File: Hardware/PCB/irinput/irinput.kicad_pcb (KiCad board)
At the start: 2 copper layers, 121 x 170.5 mm, 37 parts, among them J2 Synth_power_2x5, J3 Conn_01x06, J4 Conn_01x06, J5 AudioJack2, J6 AudioJack2, Q1 TOPS-050, SW1 SW_DPDT_x2, SW2 SW_SPDT, U1 TL074

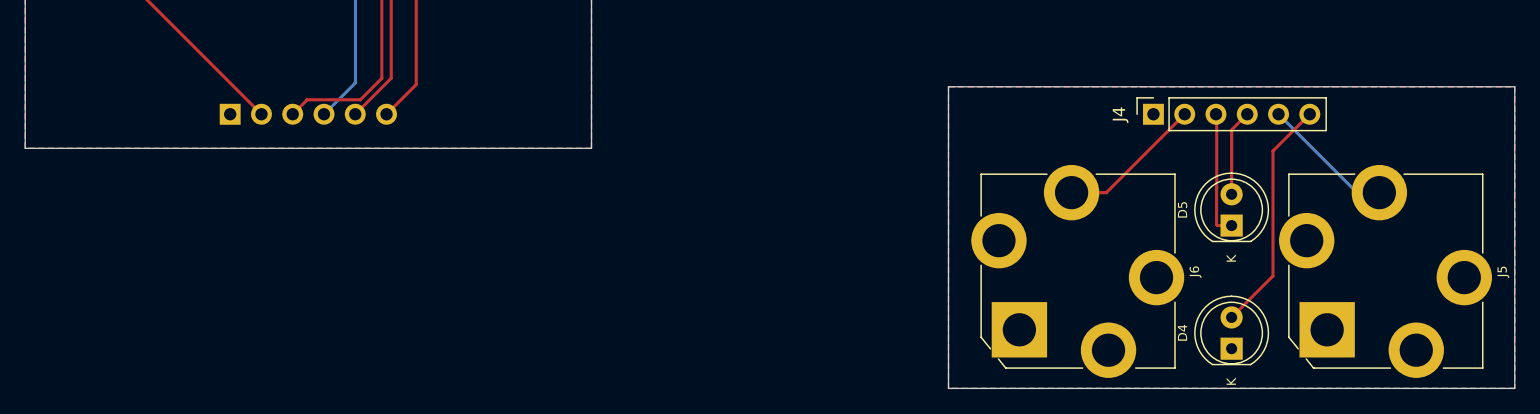
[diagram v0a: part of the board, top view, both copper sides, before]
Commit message: Revised schematic to buffer input to variable gain stage
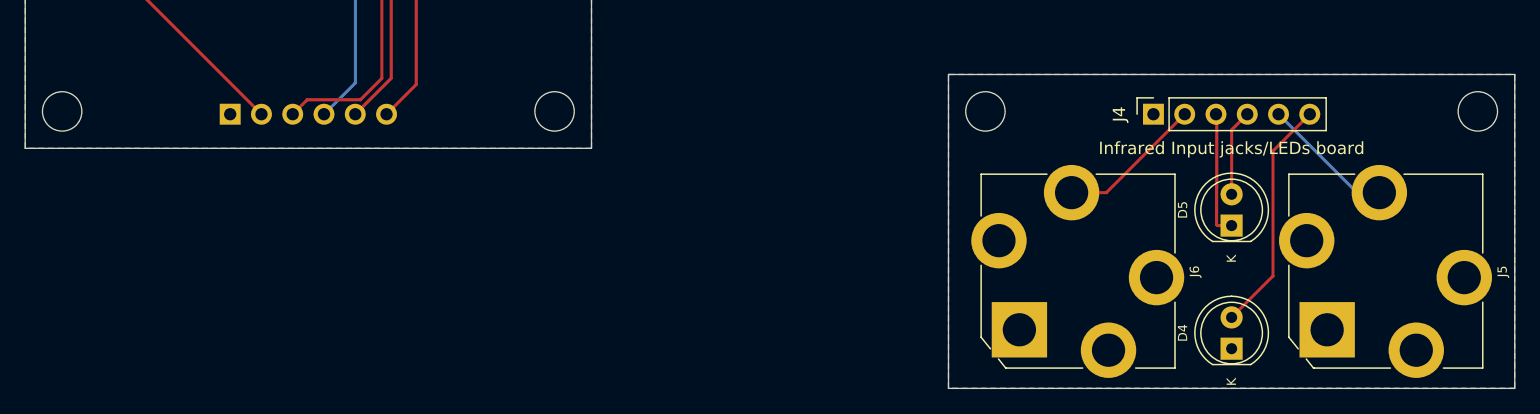
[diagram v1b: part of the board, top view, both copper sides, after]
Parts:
- added H1: MountingHole, ao_tht:MountingHole_3.2mm_M3, F.Cu at (80.0, 162.0)
- added H2: MountingHole, ao_tht:MountingHole_3.2mm_M3, F.Cu at (120.0, 162.0)
- added H3: MountingHole, ao_tht:MountingHole_3.2mm_M3, F.Cu at (155.0, 162.0)
- added H4: MountingHole, ao_tht:MountingHole_3.2mm_M3, F.Cu at (195.0, 162.0)
- moved B2 1.00 mm to (162.5, 159.0)
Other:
- outline, holes or cut-outs redrawn
- board text added: "Infrared Input"
- board text added: "Infrared Input jacks/LEDs board"
- board text added: "Main board"
- board text added: "Original design by Michael Barton Modifications by Rich Holmes Feb 2022"
- board text added: "https://www.bartonmusicalcircuits.com/irin/index.html https://github.com/holmesrichards/irinput"
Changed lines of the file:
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@@
   )
   (footprint "ao_tht:Board_Marker" (layer "F.Cu")
-    (at 162.5 160)
+    (at 162.5 159)
     (descr "Mark board for extraction")
     (property "Config" "DNF")
@@
     )
   )
+  (footprint "ao_tht:MountingHole_3.2mm_M3" (layer "F.Cu")
+    (at 80 162)
+    (descr "Mounting Hole 3.2mm, no annular, M3")
+    (tags "mounting hole 3.2mm no annular m3")
+    (property "Config" "DNF")
+    (property "Sheetfile" "irinput.kicad_sch")
+    (property "Sheetname" "")
+    (property "exclude_from_bom" "")
+    (attr exclude_from_pos_files exclude_from_bom)
+    (fp_text reference "H1" (at 0 -4.2) (layer "F.SilkS") hide
+      (effects (font (size 1 1) (thickness 0.15)))
+    )
+    (fp_text value "MountingHole" (at 0 4.2) (layer "F.Fab")
+      (effects (font (size 1 1) (thickness 0.15)))
+    )
+    (fp_text user "${REFERENCE}" (at 0.3 0) (layer "F.Fab") hide
+      (effects (font (size 1 1) (thickness 0.15)))
+    )
+    (fp_circle (center 0 0) (end 3.2 0) (layer "Cmts.User") (width 0.15) (fill none))
+    (fp_circle (center 0 0) (end 3.45 0) (layer "F.CrtYd") (width 0.05) (fill none))
+    (pad "" np_thru_hole circle locked (at 0 0) (size 3.2 3.2) (drill 3.2) (layers *.Cu *.Mask))
+  )
   (footprint "Connector_PinSocket_2.54mm:PinSocket_1x06_P2.54mm_Vertical" (layer "F.Cu")
     (at 168.65 162.23 90)
@@
     )
   )
+  (footprint "ao_tht:MountingHole_3.2mm_M3" (layer "F.Cu")
+    (at 195 162)
+    (descr "Mounting Hole 3.2mm, no annular, M3")
+    (tags "mounting hole 3.2mm no annular m3")
+    (property "Config" "DNF")
+    (property "Sheetfile" "irinput.kicad_sch")
+    (property "Sheetname" "")
+    (property "exclude_from_bom" "")
+    (attr exclude_from_pos_files exclude_from_bom)
+    (fp_text reference "H4" (at 0 -4.2) (layer "F.SilkS") hide
+      (effects (font (size 1 1) (thickness 0.15)))
+    )
+    (fp_text value "MountingHole" (at 0 4.2) (layer "F.Fab")
+      (effects (font (size 1 1) (thickness 0.15)))
+    )
+    (fp_text user "${REFERENCE}" (at 0.3 0) (layer "F.Fab") hide
+      (effects (font (size 1 1) (thickness 0.15)))
+    )
+    (fp_circle (center 0 0) (end 3.2 0) (layer "Cmts.User") (width 0.15) (fill none))
+    (fp_circle (center 0 0) (end 3.45 0) (layer "F.CrtYd") (width 0.05) (fill none))
+    (pad "" np_thru_hole circle locked (at 0 0) (size 3.2 3.2) (drill 3.2) (layers *.Cu *.Mask))
+  )
   (footprint "ao_tht:Potentiometer_Alpha_RD901F-40-00D_Single_Vertical_centered" (layer "F.Cu")
     (at 100 145)
@@
     )
   )
+  (footprint "ao_tht:MountingHole_3.2mm_M3" (layer "F.Cu")
+    (at 120 162)
+    (descr "Mounting Hole 3.2mm, no annular, M3")
+    (tags "mounting hole 3.2mm no annular m3")
+    (property "Config" "DNF")
+    (property "Sheetfile" "irinput.kicad_sch")
+    (property "Sheetname" "")
+    (property "exclude_from_bom" "")
+    (attr exclude_from_pos_files exclude_from_bom)
+    (fp_text reference "H2" (at 0 -4.2) (layer "F.SilkS") hide
+      (effects (font (size 1 1) (thickness 0.15)))
+    )
+    (fp_text value "MountingHole" (at 0 4.2) (layer "F.Fab")
+      (effects (font (size 1 1) (thickness 0.15)))
+    )
+    (fp_text user "${REFERENCE}" (at 0.3 0) (layer "F.Fab") hide
+      (effects (font (size 1 1) (thickness 0.15)))
+    )
+    (fp_circle (center 0 0) (end 3.2 0) (layer "Cmts.User") (width 0.15) (fill none))
+    (fp_circle (center 0 0) (end 3.45 0) (layer "F.CrtYd") (width 0.05) (fill none))
+    (pad "" np_thru_hole circle locked (at 0 0) (size 3.2 3.2) (drill 3.2) (layers *.Cu *.Mask))
+  )
+  (footprint "ao_tht:MountingHole_3.2mm_M3" (layer "F.Cu")
+    (at 155 162)
+    (descr "Mounting Hole 3.2mm, no annular, M3")
+    (tags "mounting hole 3.2mm no annular m3")
+    (property "Config" "DNF")
+    (property "Sheetfile" "irinput.kicad_sch")
+    (property "Sheetname" "")
+    (property "exclude_from_bom" "")
+    (attr exclude_from_pos_files exclude_from_bom)
+    (fp_text reference "H3" (at 0 -4.2) (layer "F.SilkS") hide
+      (effects (font (size 1 1) (thickness 0.15)))
+    )
+    (fp_text value "MountingHole" (at 0 4.2) (layer "F.Fab")
+      (effects (font (size 1 1) (thickness 0.15)))
+    )
+    (fp_text user "${REFERENCE}" (at 0.3 0) (layer "F.Fab") hide
+      (effects (font (size 1 1) (thickness 0.15)))
+    )
+    (fp_circle (center 0 0) (end 3.2 0) (layer "Cmts.User") (width 0.15) (fill none))
+    (fp_circle (center 0 0) (end 3.45 0) (layer "F.CrtYd") (width 0.05) (fill none))
+    (pad "" np_thru_hole circle locked (at 0 0) (size 3.2 3.2) (drill 3.2) (layers *.Cu *.Mask))
+  )
   (footprint "ao_tht:SPDT-toggle-switch-1M-series" (layer "F.Cu")
     (at 87.5 105 180)
@@
     (fp_line (start 11.21 -1.5) (end 11.21 1.5) (layer "B.CrtYd") (width 0.05))
     (fp_line (start -1.05 -1.5) (end 11.21 -1.5) (layer "B.CrtYd") (width 0.05))
+    (fp_line (start 1.93 1.25) (end 1.93 -1.25) (layer "B.Fab") (width 0.1))
     (fp_line (start 8.23 -1.25) (end 8.23 1.25) (layer "B.Fab") (width 0.1))
     (fp_line (start 8.23 1.25) (end 1.93 1.25) (layer "B.Fab") (width 0.1))
     (fp_line (start 1.93 -1.25) (end 8.23 -1.25) (layer "B.Fab") (width 0.1))
-    (fp_line (start 1.93 1.25) (end 1.93 -1.25) (layer "B.Fab") (width 0.1))
     (fp_line (start 0 0) (end 1.93 0) (layer "B.Fab") (width 0.1))
     (fp_line (start 10.16 0) (end 8.23 0) (layer "B.Fab") (width 0.1))
@@
     )
   )
+  (gr_rect (start 122 16) (end 96 27) (layer "B.SilkS") (width 0.15) (fill none))
   (gr_line (start 100 188) (end 100 14) (layer "Eco2.User") (width 0.1))
   (gr_line (start 148 188) (end 148 14) (layer "Eco2.User") (width 0.1))
@@
   (gr_line (start 95 14) (end 123 14) (layer "Edge.Cuts") (width 0.1))
   (gr_line (start 77 165) (end 77 50) (layer "Edge.Cuts") (width 0.1))
-  (gr_rect (start 198 160) (end 152 184.5) (layer "Edge.Cuts") (width 0.1) (fill none))
+  (gr_rect (start 198 159) (end 152 184.5) (layer "Edge.Cuts") (width 0.1) (fill none))
   (gr_line (start 123 165) (end 77 165) (layer "Edge.Cuts") (width 0.1))
   (gr_line (start 95 50) (end 95 14) (layer "Edge.Cuts") (width 0.1))
   (gr_line (start 123 14) (end 123 165) (layer "Edge.Cuts") (width 0.1))
+  (gr_text "Main board" (at 109 28) (layer "B.SilkS")
+    (effects (font (size 1 1) (thickness 0.15)) (justify mirror))
+  )
+  (gr_text "Infrared\nInput" (at 109 19) (layer "B.SilkS")
+    (effects (font (size 1.5 1.5) (thickness 0.3)) (justify mirror))
+  )
+  (gr_text "https://www.bartonmusicalcircuits.com/irin/index.html\nhttps://github.com/holmesrichards/irinput" (at 99 156) (layer "B.SilkS")
+    (effects (font (size 1 1) (thickness 0.15)) (justify mirror))
+  )
+  (gr_text "Original design by Michael Barton\nModifications by Rich Holmes\nFeb 2022\n" (at 109 24) (layer "B.SilkS")
+    (effects (font (size 1 1) (thickness 0.1)) (justify mirror))
+  )
+  (gr_text "Infrared Input jacks/LEDs board" (at 175 165) (layer "F.SilkS")
+    (effects (font (size 1 1) (thickness 0.15)))
+  )
   (dimension (type aligned) (layer "Eco2.User")
     (pts (xy 52 188) (xy 52 14))
@@
         (xy 198 184.5)
         (xy 152 184.5)
-        (xy 152 160)
-        (xy 198 160)
+        (xy 152 159)
+        (xy 198 159)
       )
     )

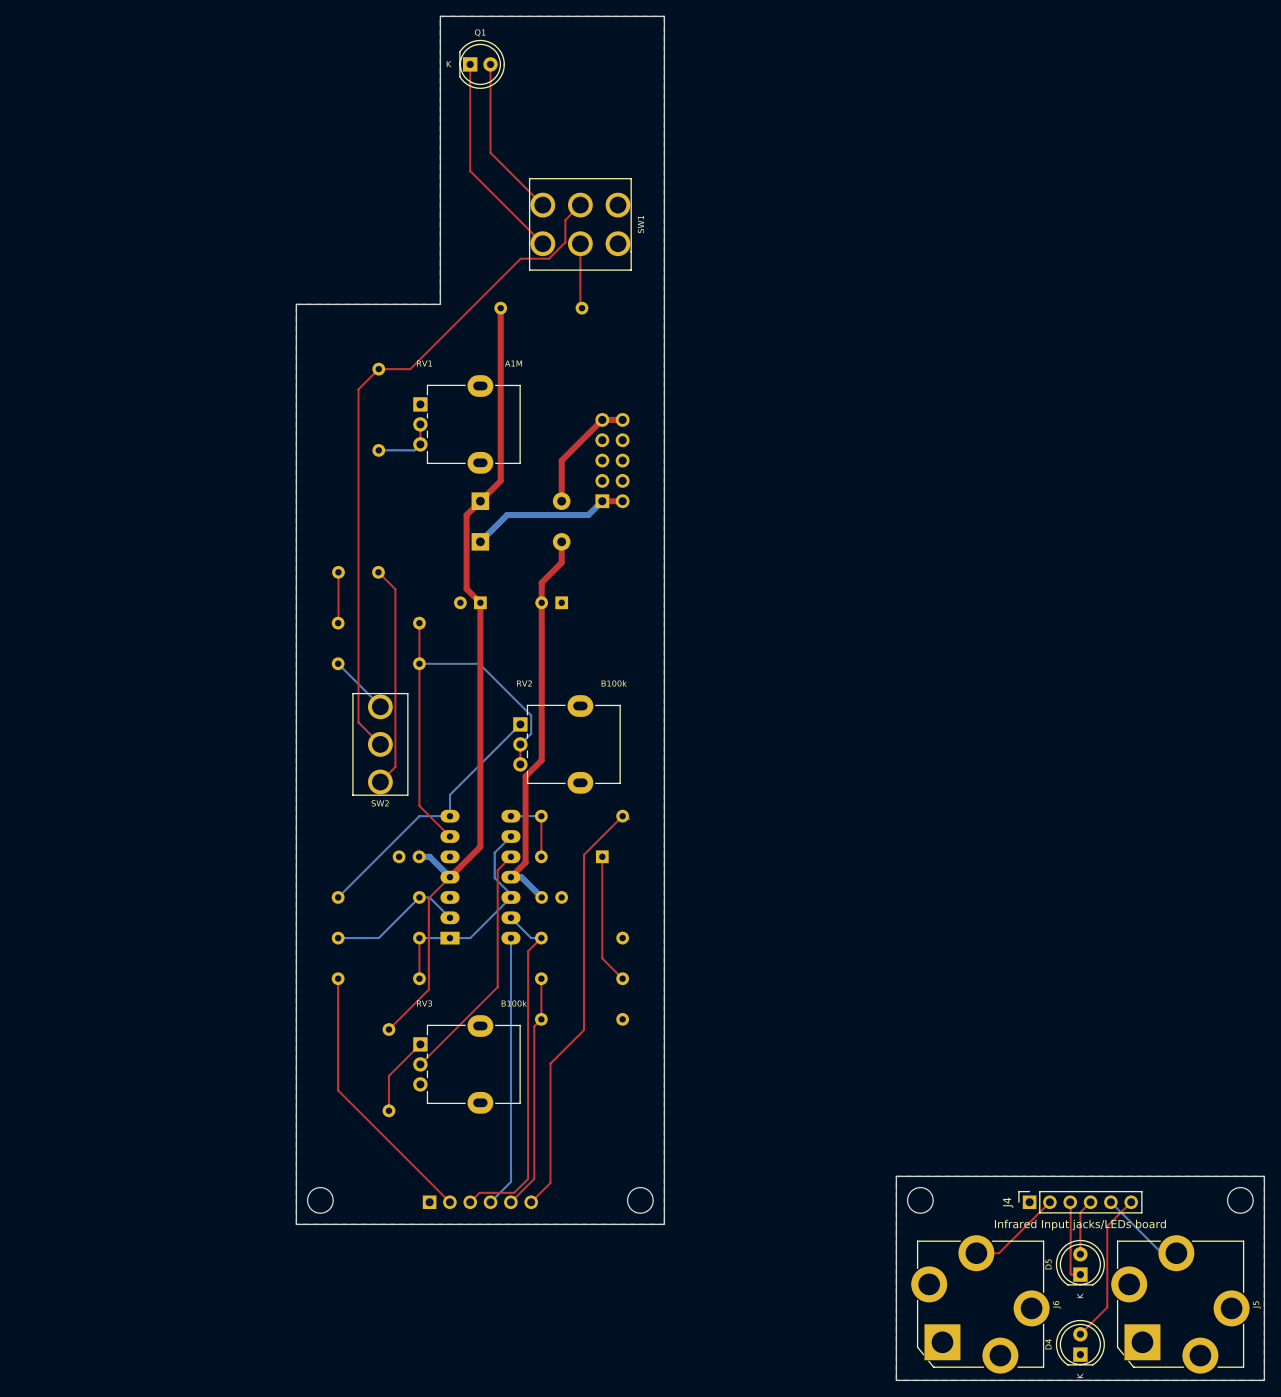
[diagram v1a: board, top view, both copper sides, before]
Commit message: Revert to using no inverting stages, put gain control on non inverting stage. Add saturation LED.
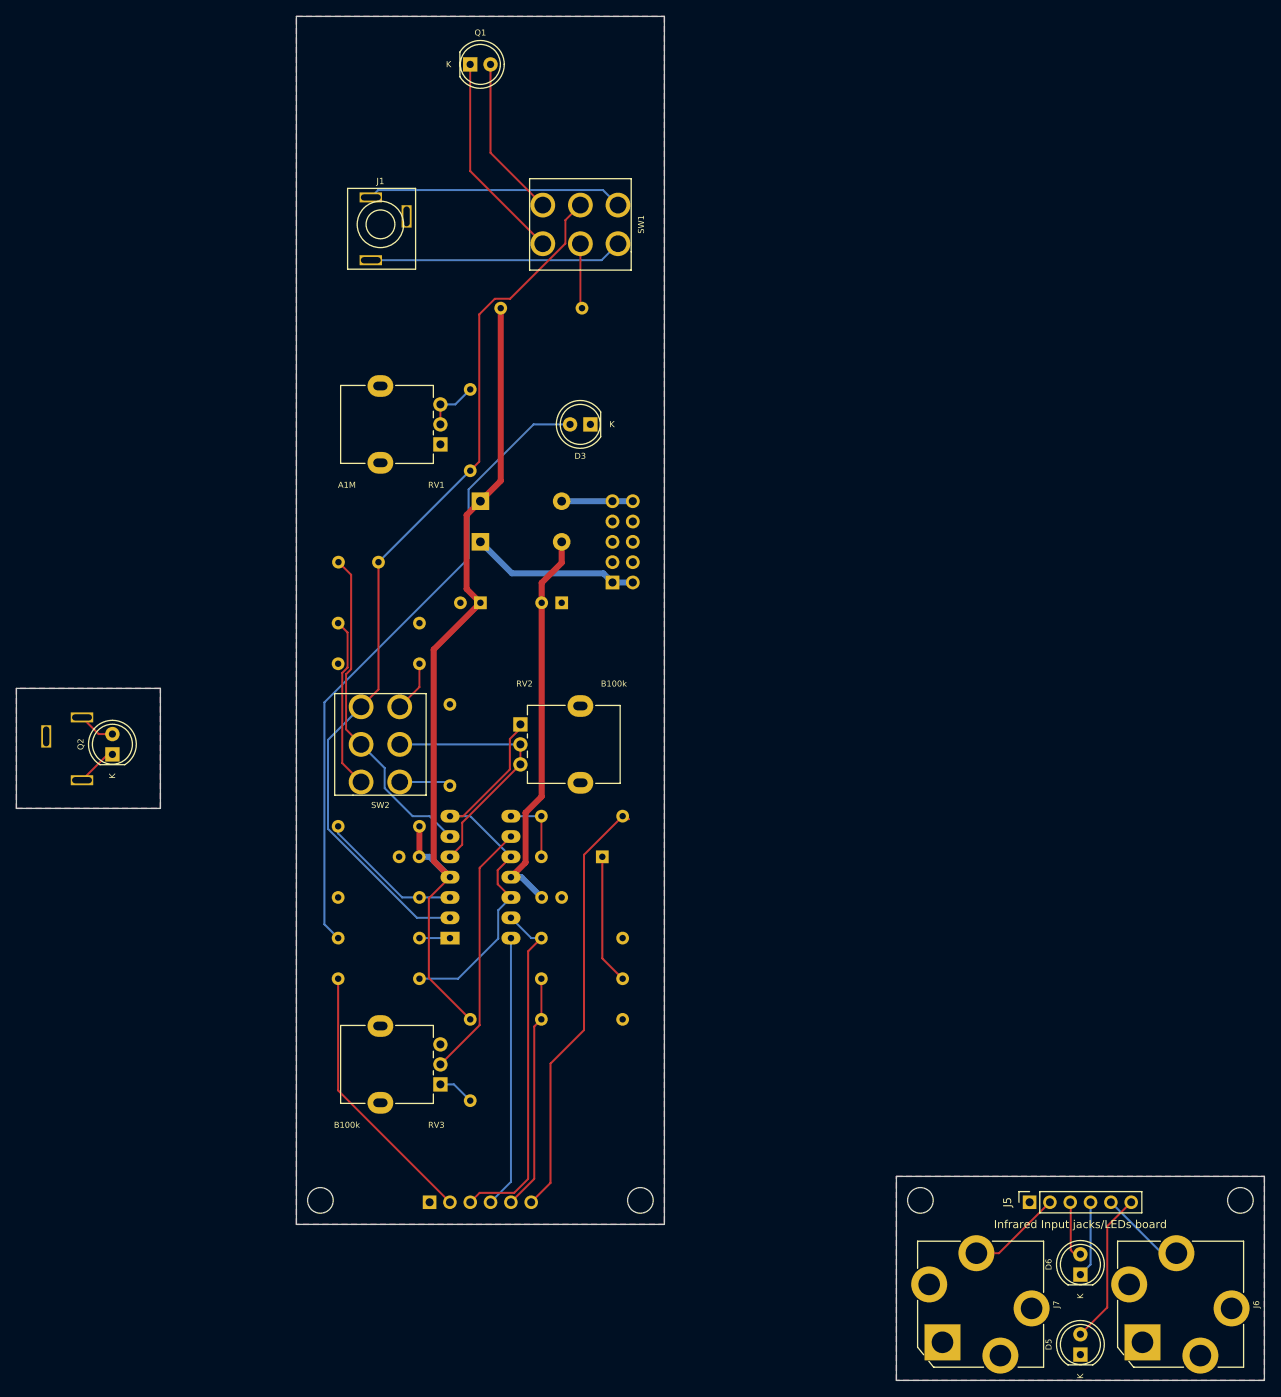
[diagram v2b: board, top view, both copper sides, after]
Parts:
- removed the R12 at (117.8, 129.2)
- added B2: Board, ao_tht:Board_Marker, F.Cu at (53.0, 98.0)
- added D3: LED_red, ao_tht:LED_D5.0mm, F.Cu at (113.8, 65.0)
- added J1: AudioJack3, ao_tht:Jack_3.5mm_PJ-301CM, F.Cu at (87.5, 40.0)
- added J3: AudioJack3, ao_tht:Jack_3.5mm_PJ-301CM, B.Cu at (49.0, 105.0)
- added Q2: TOPS-050, ao_tht:LED_D5.0mm, F.Cu at (54.0, 106.2)
- added R11: 1k, ao_tht:R_Axial_DIN0207_L6.3mm_D2.5mm_P10.16mm_Horizontal, B.Cu at (107.6, 129.2)
- added R7: 10k, ao_tht:R_Axial_DIN0207_L6.3mm_D2.5mm_P10.16mm_Horizontal, B.Cu at (96.2, 110.2)
- added R8: 2.2k, ao_tht:R_Axial_DIN0207_L6.3mm_D2.5mm_P10.16mm_Horizontal, B.Cu at (92.4, 129.2)
- R3: value 100k -> 68k
- R4, R5: value 10k -> 100k
- R6: value 10k -> 18k
- SW2: value SW_SPDT -> SW_DPDT_x2; footprint ao_tht:SPDT-toggle-switch-1M-series -> ao_tht:DPDT-toggle-switch-1M-seriesx
- moved B1 36.2 mm to (92.4, 13.9)
- moved R3 30.9 mm to (82.2, 124.1), turned to 0 degrees
- moved R5 29.2 mm to (92.4, 94.9)
- moved R6 17.3 mm to (82.2, 115.2), turned to 0 degrees
- moved R1 17.1 mm to (98.7, 70.8), turned to 90 degrees
- moved RV1 12.5 mm to (87.5, 65.0), turned to 180 degrees
- moved RV3 12.5 mm to (87.5, 145.0), turned to 180 degrees
- moved J2 10.2 mm to (116.5, 84.8)
- moved R10 10.2 mm to (98.7, 139.4)
- moved R4 10.2 mm to (82.2, 89.8), turned to 0 degrees
- moved C1 1.27 mm to (87.3, 82.2)
- renumbered B2 to B3, D3 to D4, D4 to D5, D5 to D6, J3 to J4, J4 to J5, J5 to J6, J6 to J7, R7 to R10, R9 to R12, R10 to R13, R11 to R14, R8 to R9
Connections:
- C1 pad 1: /AC -> /DC
- D6 pad 1: /CV_LED_2_P -> /CV_LED_1_P
- D6 pad 2: /CV_LED_1_P -> /CV_LED_2_P
- R1 pad 1: /EMIT -> /DC
- R3 pad 1: Net-(R3-Pad1) -> GND
- R3 pad 2: /DC -> Net-(R3-Pad2)
- R4 pad 1: Net-(R3-Pad1) -> /AC
- R4 pad 2: Net-(C1-Pad2) -> GND
- R5 pad 2: /GAIN -> GND
- R6 pad 1: Net-(R6-Pad1) -> Net-(R3-Pad2)
- R6 pad 2: Net-(R5-Pad1) -> +12V
- R9 pad 1: Net-(R6-Pad1) -> Net-(R9-Pad1)
- RV2 pad 1: /GAIN -> Net-(R9-Pad1)
- RV2 pad 2: Net-(R3-Pad1) -> Net-(RV2-Pad2)
- RV2 pad 3: Net-(R3-Pad1) -> Net-(RV2-Pad2)
- SW1 pad 5: /EMIT -> /DC
- SW2 pad 2: /EMIT -> Net-(C1-Pad2)
- U1 pad 1: Net-(R6-Pad1) -> Net-(R8-Pad1)
- U1 pad 10: /THRESHOLD -> Net-(R9-Pad1)
- U1 pad 12: Net-(R6-Pad1) -> Net-(R9-Pad1)
- U1 pad 2: Net-(R5-Pad1) -> /DC
- U1 pad 3: GND -> Net-(R3-Pad2)
- U1 pad 5: GND -> Net-(RV2-Pad2)
- U1 pad 6: Net-(R3-Pad1) -> Net-(C1-Pad2)
- U1 pad 7: /GAIN -> Net-(R9-Pad1)
- U1 pad 9: Net-(R6-Pad1) -> /THRESHOLD
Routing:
- net /DC: track 7.47 -> 112.0 mm
- net /EMIT: track 84.4 -> 0.00 mm
- net Net-(D3-Pad2): track 0.00 -> 80.3 mm
- net Net-(R3-Pad1): track 51.6 -> 0.00 mm
- net Net-(R9-Pad1): track 0.00 -> 50.0 mm
- net Net-(C1-Pad2): track 6.31 -> 41.8 mm
- net /GAIN: track 33.3 -> 0.00 mm
- net Net-(RV2-Pad2): track 0.00 -> 32.8 mm
- net /EXT_E: track 0.00 -> 32.1 mm
- net /EXT_C: track 0.00 -> 31.8 mm
- net Net-(R6-Pad1): track 28.1 -> 0.00 mm
- net Net-(R3-Pad2): track 0.00 -> 18.2 mm
- net Net-(R5-Pad1): track 17.1 -> 6.40 mm
- net Net-(R7-Pad1): track 0.00 -> 6.47 mm
- net /AC: track 27.9 -> 21.6 mm
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- added copper zone on B.Cu, net GND2
- added copper zone on F.Cu, net GND2
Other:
- board size 121 x 170.5 mm -> 156 x 170.5 mm
